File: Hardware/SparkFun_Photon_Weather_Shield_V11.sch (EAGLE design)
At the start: 44 parts, among them U1 3.3V MIC5219, U2 SI7021, U3 MPL3115A2LGA8

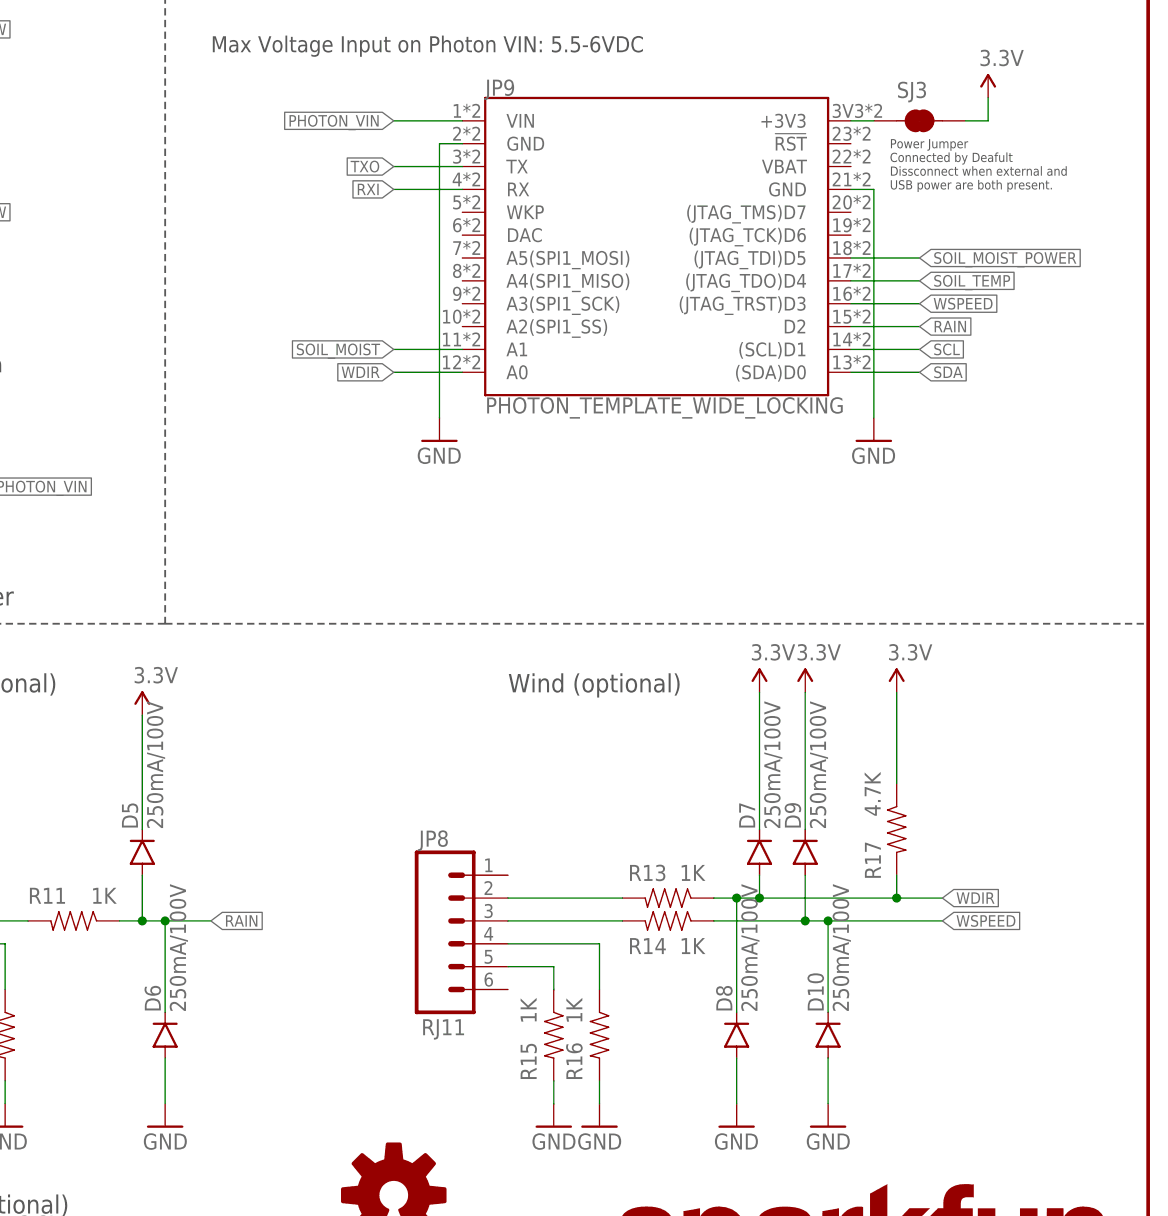
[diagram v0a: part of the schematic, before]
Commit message: Final ENG_Checklist before ordering REDs
Fixed two issues: misspelling and overlapping values on nets.. Pushing
for Reds.
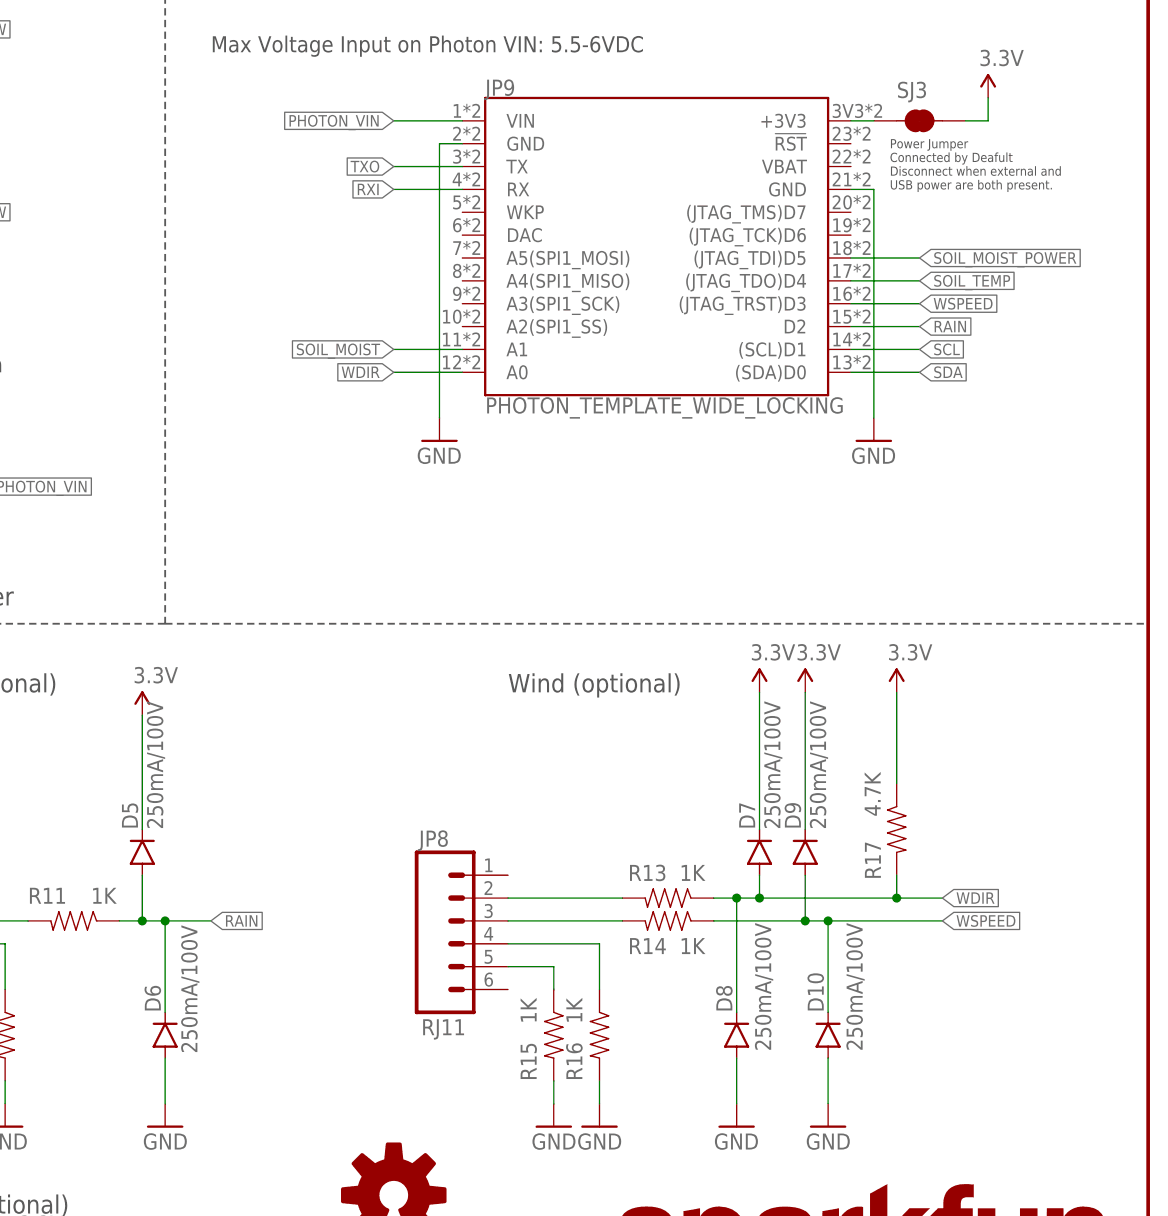
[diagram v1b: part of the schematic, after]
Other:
- note added: "Power Jumper Connected by Deafult Disconnect when external and USB power are both present."
- note removed: "Power Jumper Connected by Deafult Dissconnect when external and USB power are both present."
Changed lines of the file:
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@@
 <text x="220.218" y="157.48" size="1.016" layer="97" font="vector">Power Jumper
 Connected by Deafult
-Dissconnect when external and
+Disconnect when external and
 USB power are both present. </text>
 <text x="47.752" y="119.888" size="2.032" layer="97" font="vector">Serial 1 Port (optional)</text>
@@
 <attribute name="VALUE" x="196.85" y="80.645" size="1.778" layer="96" font="vector"/>
 </instance>
-<instance part="D9" gate="G$1" x="210.82" y="83.82" rot="R90"/>
-<instance part="D10" gate="G$1" x="213.36" y="63.5" rot="R90"/>
-<instance part="D7" gate="G$1" x="205.74" y="83.82" rot="R90"/>
-<instance part="D8" gate="G$1" x="203.2" y="63.5" rot="R90"/>
-<instance part="D5" gate="G$1" x="137.16" y="83.82" rot="R90"/>
-<instance part="D6" gate="G$1" x="139.7" y="63.5" rot="R90"/>
+<instance part="D9" gate="G$1" x="210.82" y="83.82" smashed="yes" rot="R90">
+<attribute name="NAME" x="210.3374" y="86.36" size="1.778" layer="95" rot="R90"/>
+<attribute name="VALUE" x="213.1314" y="86.36" size="1.778" layer="96" rot="R90"/>
+</instance>
+<instance part="D10" gate="G$1" x="213.36" y="63.5" smashed="yes" rot="R90">
+<attribute name="NAME" x="212.8774" y="66.04" size="1.778" layer="95" rot="R90"/>
+<attribute name="VALUE" x="217.1954" y="61.722" size="1.778" layer="96" rot="R90"/>
+</instance>
+<instance part="D7" gate="G$1" x="205.74" y="83.82" smashed="yes" rot="R90">
+<attribute name="NAME" x="205.2574" y="86.36" size="1.778" layer="95" rot="R90"/>
+<attribute name="VALUE" x="208.0514" y="86.36" size="1.778" layer="96" rot="R90"/>
+</instance>
+<instance part="D8" gate="G$1" x="203.2" y="63.5" smashed="yes" rot="R90">
+<attribute name="NAME" x="202.7174" y="66.04" size="1.778" layer="95" rot="R90"/>
+<attribute name="VALUE" x="207.0354" y="61.722" size="1.778" layer="96" rot="R90"/>
+</instance>
+<instance part="D5" gate="G$1" x="137.16" y="83.82" smashed="yes" rot="R90">
+<attribute name="NAME" x="136.6774" y="86.36" size="1.778" layer="95" rot="R90"/>
+<attribute name="VALUE" x="139.4714" y="86.36" size="1.778" layer="96" rot="R90"/>
+</instance>
+<instance part="D6" gate="G$1" x="139.7" y="63.5" smashed="yes" rot="R90">
+<attribute name="NAME" x="139.2174" y="66.04" size="1.778" layer="95" rot="R90"/>
+<attribute name="VALUE" x="143.2814" y="61.468" size="1.778" layer="96" rot="R90"/>
+</instance>
 <instance part="GND21" gate="1" x="213.36" y="53.34" rot="MR0"/>
 <instance part="GND29" gate="1" x="203.2" y="53.34"/>

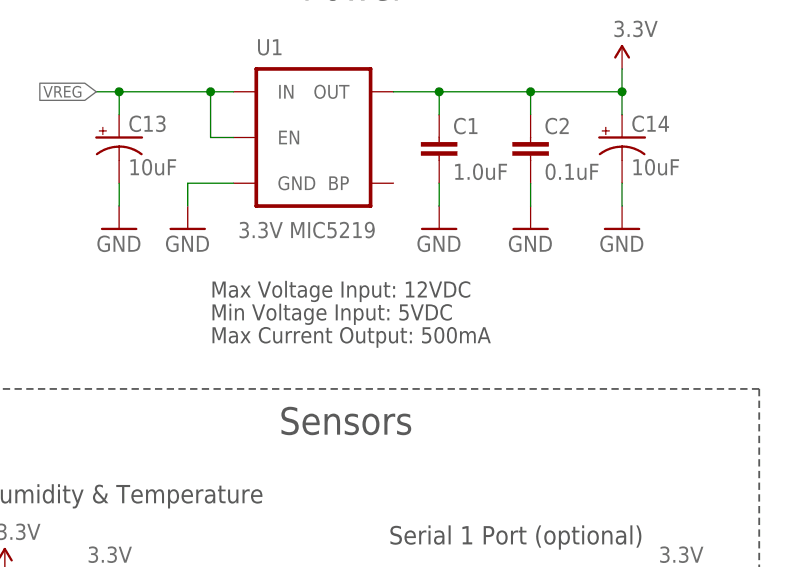
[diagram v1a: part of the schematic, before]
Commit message: Update w/ Correct Voltage Regulator Name
The schematic was updated incorrectly with the voltage regulator name and specifications. Instead of the MIC5219, it is populated with the **MIC5205**.

While the recommended operating voltage from the [datasheet](http://ww1.microchip.com/downloads/en/DeviceDoc/20005785A.pdf) is up to +16V, the actual stable voltage in real world conditions is actually about ~11.5V. This has been been tested and verified by @sfemark .
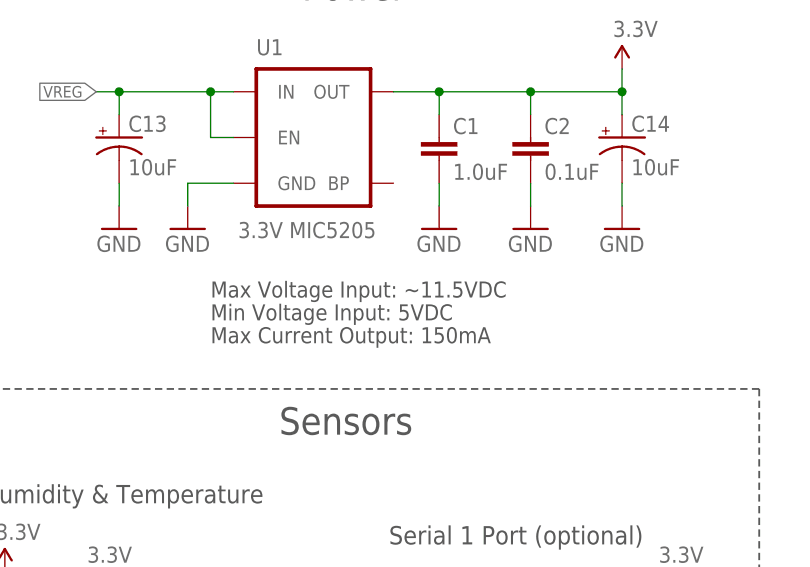
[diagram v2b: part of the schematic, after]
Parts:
- U1: value 3.3V MIC5219 -> 3.3V MIC5205
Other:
- note added: "Max Current Output: 150mA"
- note added: "Max Voltage Input: ~11.5VDC"
- note removed: "Max Current Output: 500mA"
- note removed: "Max Voltage Input: 12VDC"
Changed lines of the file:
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@@
 <part name="GND25" library="SparkFun" deviceset="GND" device=""/>
 <part name="GND26" library="SparkFun" deviceset="GND" device=""/>
-<part name="U1" library="SparkFun-PowerIC" deviceset="MIC5205" device="3.3V" value="3.3V MIC5219"/>
+<part name="U1" library="SparkFun-PowerIC" deviceset="MIC5205" device="3.3V" value="3.3V MIC5205"/>
 <part name="GND30" library="SparkFun" deviceset="GND" device=""/>
 <part name="C1" library="SparkFun-Capacitors" deviceset="1.0UF-16V-10%(0603)" device="" value="1.0uF"/>
@@
 <sheet>
 <plain>
-<text x="27.94" y="147.32" size="1.778" layer="97" font="vector">Max Voltage Input: 12VDC</text>
-<text x="27.94" y="142.24" size="1.778" layer="97" font="vector">Max Current Output: 500mA</text>
+<text x="27.94" y="147.32" size="1.778" layer="97" font="vector">Max Voltage Input: ~11.5VDC</text>
+<text x="27.94" y="142.24" size="1.778" layer="97" font="vector">Max Current Output: 150mA</text>
 <text x="35.56" y="53.34" size="1.778" layer="97" font="vector">I2C Read: 0xC1</text>
 <text x="35.56" y="50.8" size="1.778" layer="97" font="vector">I2C Write: 0xC0</text>
